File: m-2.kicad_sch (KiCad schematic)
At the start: 14 parts, among them J3 Bus_M.2_1-2199230-6, Y1 Oscillator_SMD_32.768kHz_ECS_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

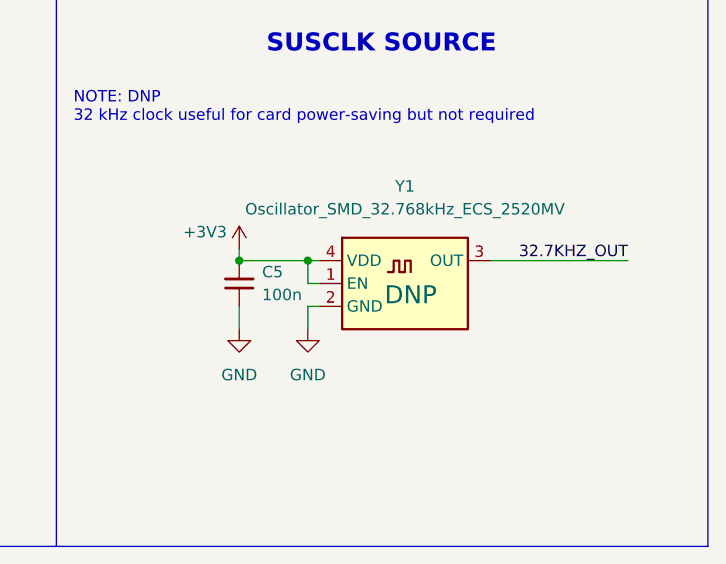
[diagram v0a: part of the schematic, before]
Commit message: [#56948] Update symbol/footprint links; Migrate to KiCad 7
[#56948] Update from lib; clean DRC

Remove Public False property from components
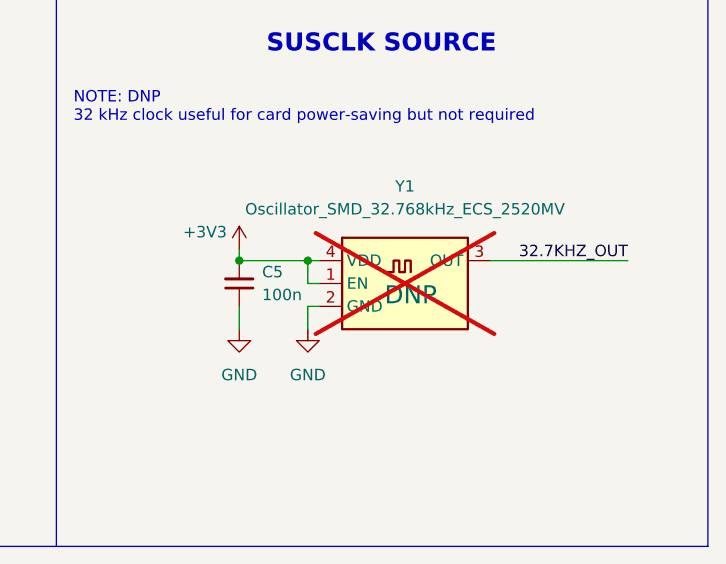
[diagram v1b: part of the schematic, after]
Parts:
- C2, C3: Manufacturer Yaego -> YAGEO
- H1, H2: footprint antmicro-footprints:Spacer_SMD_M2.5_H2.5mm_Wurth_9774025151 -> antmicro-footprints:Spacer_Drill3.7mm_H2.5mm_9774025151R; symbol antmicroMechanicalParts:Spacer_H2.5mm_9774025151 -> antmicroMechanicalParts:Spacer_Drill3.7mm_H2.5mm_9774025151R; MPN 9774025151 -> 9774025151R
- Y1: symbol antmicroOscillators:Oscillator_SMD_32.768kHz_ECS_2520MV -> antmicroOscillators:Oscillator_32.768kHz_ECS_2520MV; now not fitted

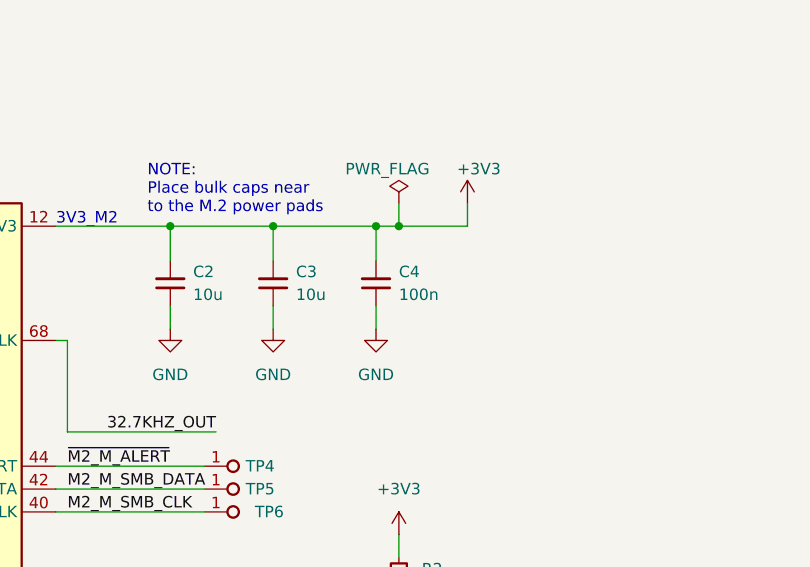
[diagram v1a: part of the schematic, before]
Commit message: [#64006] Addresed all changes suggested in PCB review
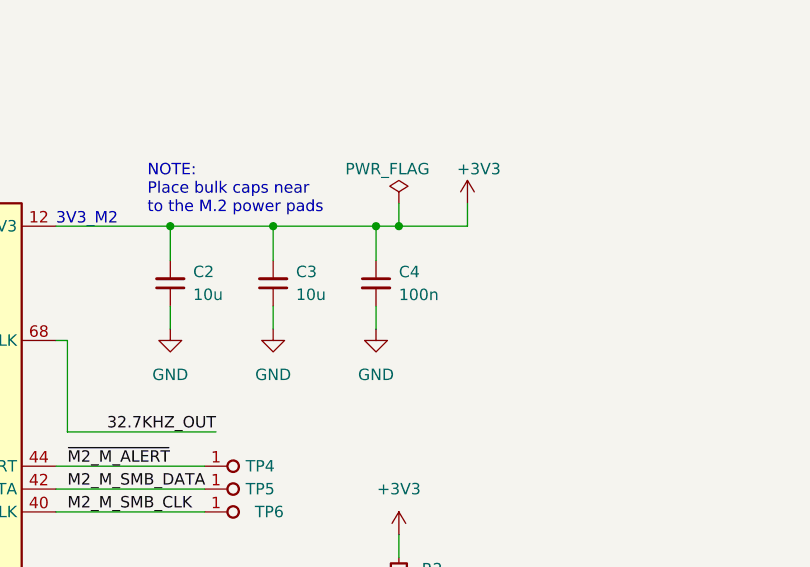
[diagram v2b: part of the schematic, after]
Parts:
- removed C4: C_100n_0603, antmicro-footprints:C_0603_1608Metric, symbol antmicroCapacitors0603:C_100n_0603
- added C4: C_100n_16V_X7R_0402, antmicro-footprints:C_0402_1005Metric, symbol antmicroCapacitors0402:C_100n_16V_X7R_0402
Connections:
- net +3V3: now also C4.1
- net GND: now also C4.2
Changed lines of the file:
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@@
+    )
+  )
+  (symbol (lib_id "antmicroCapacitors0402:C_100n_16V_X7R_0402") (at 160.02 52.07 90) (mirror x) (unit 1)
+    (in_bom yes) (on_board yes) (dnp no) (fields_autoplaced)
+    (property "Reference" "C4" (at 162.56 53.3463 90)
+      (effects (font (size 1.27 1.27) (thickness 0.15)) (justify right))
+    )
+    (property "Value" "C_100n_16V_X7R_0402" (at 182.88 67.31 0)
+      (effects (font (size 1.27 1.27) (thickness 0.15)) (justify left bottom) hide)
+    )
+    (property "Footprint" "antmicro-footprints:C_0402_1005Metric" (at 185.42 67.31 0)
+      (effects (font (size 1.27 1.27) (thickness 0.15)) (justify left bottom) hide)
+    )
+    (property "Datasheet" "https://www.kemet.com/en/us/capacitors/product/C0402C104J4RAC7411.html" (at 187.96 67.31 0)
+      (effects (font (size 1.27 1.27) (thickness 0.15)) (justify left bottom) hide)
+    )
+    (property "MPN" "C0402C104J4RAC7411" (at 190.5 67.31 0)
+      (effects (font (size 1.27 1.27) (thickness 0.15)) (justify left bottom) hide)
+    )
+    (property "Val" "100n" (at 162.56 55.8863 90)
+      (effects (font (size 1.27 1.27) (thickness 0.15)) (justify right))
+    )
+    (property "Voltage" "16V" (at 170.18 67.31 0)
+      (effects (font (size 1.27 1.27) (thickness 0.15)) (justify left bottom) hide)
+    )
+    (property "Dielectric" "X7R" (at 172.72 67.31 0)
+      (effects (font (size 1.27 1.27) (thickness 0.15)) (justify left bottom) hide)
+    )
+    (property "Manufacturer" "KEMET" (at 175.26 67.31 0)
+      (effects (font (size 1.27 1.27) (thickness 0.15)) (justify left bottom) hide)
+    )
+    (property "License" "Apache-2.0" (at 177.8 67.31 0)
+      (effects (font (size 1.27 1.27) (thickness 0.15)) (justify left bottom) hide)
+    )
+    (property "Author" "Antmicro" (at 180.34 67.31 0)
+      (effects (font (size 1.27 1.27) (thickness 0.15)) (justify left bottom) hide)
+    )
+    (pin "2")
+    (pin "1")
+    (instances
+      (project "jetson-orin-baseboard-storage-expansion"
+        (path "/45f331f1-15bc-4fff-94ad-9fb3699b0151/cc2f3977-c157-49db-9d7c-b1273851c6f6"
+          (reference "C4") (unit 1)
+        )
+      )
     )
   )
@@
         )
       )
-    )
-  )
-  (symbol (lib_id "antmicroCapacitors0603:C_100n_0603") (at 160.02 57.15 90) (unit 1)
-    (in_bom yes) (on_board yes) (dnp no) (fields_autoplaced)
-    (property "Reference" "C4" (at 162.56 53.3335 90)
-      (effects (font (size 1.27 1.27) (thickness 0.15)) (justify right))
-    )
-    (property "Value" "C_100n_0603" (at 170.18 36.83 0)
-      (effects (font (size 1.27 1.27) (thickness 0.15)) (justify left bottom) hide)
-    )
-    (property "Footprint" "antmicro-footprints:C_0603_1608Metric" (at 172.72 36.83 0)
-      (effects (font (size 1.27 1.27) (thickness 0.15)) (justify left bottom) hide)
-    )
-    (property "Datasheet" " " (at 175.26 36.83 0)
-      (effects (font (size 1.27 1.27) (thickness 0.15)) (justify left bottom) hide)
-    )
-    (property "MPN" "0603YC104KAZ2A" (at 177.8 36.83 0)
-      (effects (font (size 1.27 1.27) (thickness 0.15)) (justify left bottom) hide)
-    )
-    (property "Manufacturer" "AVX" (at 180.34 36.83 0)
-      (effects (font (size 1.27 1.27) (thickness 0.15)) (justify left bottom) hide)
-    )
-    (property "License" "Apache-2.0" (at 182.88 36.83 0)
-      (effects (font (size 1.27 1.27) (thickness 0.15)) (justify left bottom) hide)
-    )
-    (property "Author" "Antmicro" (at 185.42 36.83 0)
-      (effects (font (size 1.27 1.27) (thickness 0.15)) (justify left bottom) hide)
-    )
-    (property "Val" "100n" (at 162.56 55.8735 90)
-      (effects (font (size 1.27 1.27) (thickness 0.15)) (justify right))
-    )
-    (property "Voltage" "" (at 187.96 36.83 0)
-      (effects (font (size 1.27 1.27)) (justify left bottom) hide)
-    )
-    (property "Dielectric" "" (at 190.5 36.83 0)
-      (effects (font (size 1.27 1.27)) (justify left bottom) hide)
-    )
-    (pin "1")
-    (pin "2")
-    (instances
-      (project "jetson-orin-baseboard-storage-expansion"
-        (path "/45f331f1-15bc-4fff-94ad-9fb3699b0151/cc2f3977-c157-49db-9d7c-b1273851c6f6"
-          (reference "C4") (unit 1)
-        )
-      )
